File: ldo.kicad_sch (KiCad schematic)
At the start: 4 parts, among them U501 SPX3819M5-L-3-3

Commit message: Update to kicad 9
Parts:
- C502: value 10n -> 10n
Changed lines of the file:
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@@
 (kicad_sch
-	(version 20231120)
+	(version 20250114)
 	(generator "eeschema")
-	(generator_version "8.0")
+	(generator_version "9.0")
 	(paper "A5")
 	(junction
@@
 	(label "BYP"
 		(at 93.98 63.5 0)
-		(fields_autoplaced yes)
 		(effects
 			(font
@@
 		(shape input)
 		(at 62.23 60.96 180)
-		(fields_autoplaced yes)
 		(effects
 			(font
@@
 		(shape output)
 		(at 119.38 60.96 0)
-		(fields_autoplaced yes)
 		(effects
 			(font
@@
 			)
 		)
-		(property "Value" "10n	"
+		(property "Value" "10n"
 			(at 96.52 69.85 0)
 			(effects

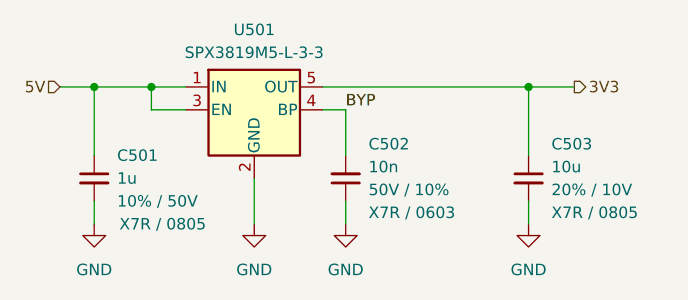
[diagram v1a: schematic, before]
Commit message: Update reference designators to single digit
Fits on the silk better
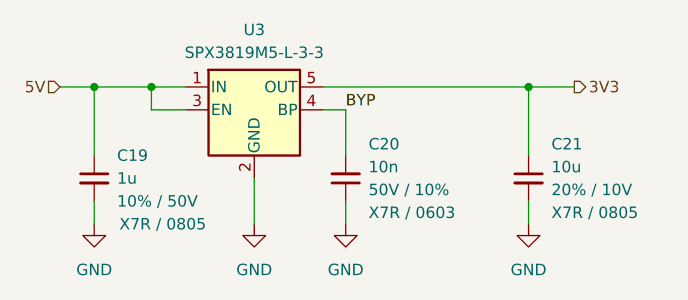
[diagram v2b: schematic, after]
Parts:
- renumbered C501 to C19, C502 to C20, C503 to C21, U501 to U3
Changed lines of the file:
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@@
 		(dnp no)
 		(fields_autoplaced yes)
-		(property "Reference" "#PWR0503"
+		(property "Reference" "#PWR033"
 			(at 93.98 82.55 0)
 			(effects
@@
 			(project "youdbetterrun"
 				(path "/50da2b4e-34b1-4787-8ee6-5d7d17f804f4/36ef99fe-a89f-4e2b-807e-d0c916080945"
-					(reference "#PWR0503")
+					(reference "#PWR033")
 					(unit 1)
 				)
@@
 		(on_board yes)
 		(dnp no)
-		(property "Reference" "C501"
+		(property "Reference" "C19"
 			(at 68.58 68.58 0)
 			(effects
@@
 			(project "youdbetterrun"
 				(path "/50da2b4e-34b1-4787-8ee6-5d7d17f804f4/36ef99fe-a89f-4e2b-807e-d0c916080945"
-					(reference "C501")
+					(reference "C19")
 					(unit 1)
 				)
@@
 		(dnp no)
 		(fields_autoplaced yes)
-		(property "Reference" "#PWR0504"
+		(property "Reference" "#PWR034"
 			(at 114.3 82.55 0)
 			(effects
@@
 			(project "youdbetterrun"
 				(path "/50da2b4e-34b1-4787-8ee6-5d7d17f804f4/36ef99fe-a89f-4e2b-807e-d0c916080945"
-					(reference "#PWR0504")
+					(reference "#PWR034")
 					(unit 1)
 				)
@@
 		(dnp no)
 		(fields_autoplaced yes)
-		(property "Reference" "U501"
+		(property "Reference" "U3"
 			(at 83.82 54.61 0)
 			(effects
@@
 			(project "youdbetterrun"
 				(path "/50da2b4e-34b1-4787-8ee6-5d7d17f804f4/36ef99fe-a89f-4e2b-807e-d0c916080945"
-					(reference "U501")
+					(reference "U3")
 					(unit 1)
 				)
@@
 		(on_board yes)
 		(dnp no)
-		(property "Reference" "C502"
+		(property "Reference" "C20"
 			(at 96.52 67.31 0)
 			(effects
@@
 			(project "youdbetterrun"
 				(path "/50da2b4e-34b1-4787-8ee6-5d7d17f804f4/36ef99fe-a89f-4e2b-807e-d0c916080945"
-					(reference "C502")
+					(reference "C20")
 					(unit 1)
 				)
@@
 		(on_board yes)
 		(dnp no)
-		(property "Reference" "C503"
+		(property "Reference" "C21"
 			(at 116.84 67.31 0)
 			(effects
@@
 			(project "youdbetterrun"
 				(path "/50da2b4e-34b1-4787-8ee6-5d7d17f804f4/36ef99fe-a89f-4e2b-807e-d0c916080945"
-					(reference "C503")
+					(reference "C21")
 					(unit 1)
 				)
@@
 		(dnp no)
 		(fields_autoplaced yes)
-		(property "Reference" "#PWR0501"
+		(property "Reference" "#PWR031"
 			(at 66.04 82.55 0)
 			(effects
@@
 			(project "youdbetterrun"
 				(path "/50da2b4e-34b1-4787-8ee6-5d7d17f804f4/36ef99fe-a89f-4e2b-807e-d0c916080945"
-					(reference "#PWR0501")
+					(reference "#PWR031")
 					(unit 1)
 				)
@@
 		(dnp no)
 		(fields_autoplaced yes)
-		(property "Reference" "#PWR0502"
+		(property "Reference" "#PWR032"
 			(at 83.82 82.55 0)
 			(effects
@@
 			(project "youdbetterrun"
 				(path "/50da2b4e-34b1-4787-8ee6-5d7d17f804f4/36ef99fe-a89f-4e2b-807e-d0c916080945"
-					(reference "#PWR0502")
-					(unit 1)
-				)
+					(reference "#PWR032")
+					(unit 1)
+				)

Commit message: Lighthouse
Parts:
- added C8, C9: 22u, Capacitor_THT:C_Radial_D5.0mm_H5.0mm_P2.00mm, symbol Device:C_Polarized_Small
- added D2, D3: MBR120, Diode_SMD:D_SOD-123F, symbol Device:D_Schottky_Small
- added J5: 694106301002, Connector_BarrelJack:BarrelJack_Wuerth_6941xx301002, symbol Connector:Barrel_Jack_Switch
- added J6: From_E-stop, TerminalBlock:TerminalBlock_MaiXu_MX126-5.0-02P_1x02_P5.00mm, symbol Connector:Screw_Terminal_01x02
- added U4: R-78E5.0-1.0, Converter_DCDC:Converter_DCDC_RECOM_R-78E-0.5_THT, symbol Regulator_Switching:R-78E3.3-1.0
- renumbered C19 to C10, C20 to C11, C21 to C12, U3 to U5
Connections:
- net 5V: now also D2.1 (K), D3.1 (K)
- net GND: now also C8.2, C9.2, J5.2, J5.3, J6.2 (Pin_2), U4.2 (GND)
- new net PWR: C8.1, J5.1, J6.1 (Pin_1), U4.1 (IN)
- new net VREG_OUT: C9.1, D3.2 (A), U4.3 (OUT)
- new net VUSB: D2.2 (A)
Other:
- company: (none) -> Marcel Robitaille
- title: (none) -> Power
- moved on the sheet: C10, C11, C12, U5

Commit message: Termianl block 3d view
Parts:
- J6: value From_E-stop -> TB0010-500-02GR; footprint TerminalBlock:TerminalBlock_MaiXu_MX126-5.0-02P_1x02_P5.00mm -> lighthouse:TerminalBlock_TB0010-500-02GR_1x02_P5.00mm
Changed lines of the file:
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@@
 			)
 		)
-		(property "Value" "From_E-stop"
+		(property "Value" "TB0010-500-02GR"
 			(at 35.56 44.45 0)
 			(effects
@@
 			)
 		)
-		(property "Footprint" "TerminalBlock:TerminalBlock_MaiXu_MX126-5.0-02P_1x02_P5.00mm"
+		(property "Footprint" "lighthouse:TerminalBlock_TB0010-500-02GR_1x02_P5.00mm"
 			(at 35.56 48.26 0)
 			(effects

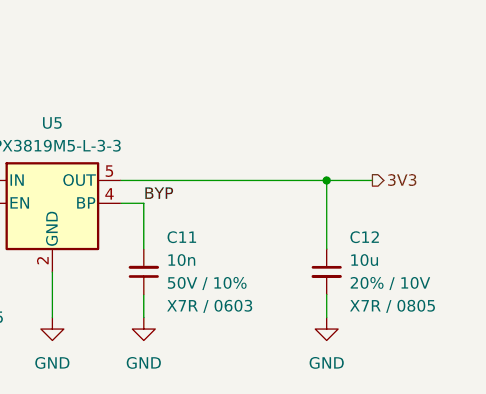
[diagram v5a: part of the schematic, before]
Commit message: Add component attributes
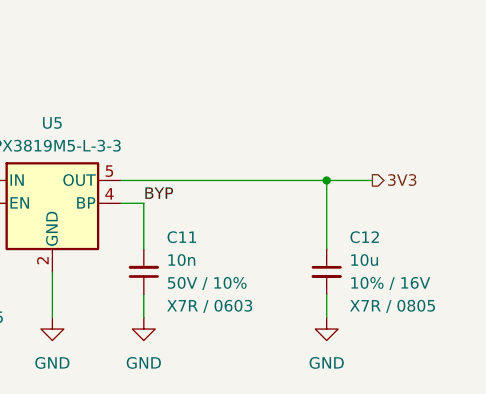
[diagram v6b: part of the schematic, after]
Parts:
- C12: LCSC Part Number C5189822 -> (none); MPN CS2012X7R106M100NRE -> CL21A106KOQNNNE; Manufacturer Samwha Capacitor -> Samsung Electro-Mechanics; Mouser Part Number (none) -> 187-CL21A106KOQNNNE; Rated Voltage 10V -> 16V; Tolerance 20% -> 10%
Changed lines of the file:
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@@
+			)
+		)
+		(property "Manufactuer" ""
+			(at 101.6 71.12 0)
+			(effects
+				(font
+					(size 1.27 1.27)
+				)
+				(hide yes)
 			)
 		)
@@
 			)
 		)
+		(property "Manufactuer" ""
+			(at 53.34 66.04 0)
+			(effects
+				(font
+					(size 1.27 1.27)
+				)
+				(hide yes)
+			)
+		)
 		(pin "2"
 		)
@@
 			)
 		)
+		(property "Manufactuer" ""
+			(at 73.66 66.04 0)
+			(effects
+				(font
+					(size 1.27 1.27)
+				)
+				(hide yes)
+			)
+		)
 		(pin "2"
 		)
@@
 			)
 		)
+		(property "Manufactuer" ""
+			(at 86.36 60.96 0)
+			(effects
+				(font
+					(size 1.27 1.27)
+				)
+				(hide yes)
+			)
+		)
 		(pin "2"
 		)
@@
 			)
 		)
+		(property "Manufactuer" ""
+			(at 33.02 63.5 0)
+			(effects
+				(font
+					(size 1.27 1.27)
+				)
+				(hide yes)
+			)
+		)
 		(pin "2"
 		)
@@
 			)
 		)
+		(property "Manufactuer" ""
+			(at 35.56 48.26 0)
+			(effects
+				(font
+					(size 1.27 1.27)
+				)
+				(hide yes)
+			)
+		)
 		(pin "1"
 		)
@@
 			)
 		)
+		(property "Manufactuer" ""
+			(at 86.36 50.8 0)
+			(effects
+				(font
+					(size 1.27 1.27)
+				)
+				(hide yes)
+			)
+		)
 		(pin "2"
 		)
@@
 			)
 		)
+		(property "Manufactuer" ""
+			(at 63.5 60.96 0)
+			(effects
+				(font
+					(size 1.27 1.27)
+				)
+				(hide yes)
+			)
+		)
 		(pin "3"
 		)
@@
 			)
 		)
+		(property "Manufactuer" ""
+			(at 119.38 63.5 0)
+			(effects
+				(font
+					(size 1.27 1.27)
+				)
+				(hide yes)
+			)
+		)
 		(pin "1"
 		)
@@
 		)
 		(property "Tolerance" "10%"
+			(at 129.54 71.12 0)
+			(effects
+				(font
+					(size 1.27 1.27)
+				)
+				(hide yes)
+			)
+		)
+		(property "Manufactuer" ""
 			(at 129.54 71.12 0)
 			(effects
@@
 			)
 		)
-		(property "LCSC Part Number" "C5189822"
+		(property "LCSC Part Number" ""
 			(at 149.86 71.12 0)
 			(effects
@@
 			)
 		)
-		(property "MPN" "CS2012X7R106M100NRE"
+		(property "MPN" "CL21A106KOQNNNE"
 			(at 149.86 71.12 0)
 			(effects
@@
 			)
 		)
-		(property "Manufacturer" "Samwha Capacitor"
+		(property "Manufacturer" "Samsung Electro-Mechanics"
 			(at 149.86 71.12 0)
 			(effects
@@
 			)
 		)
-		(property "Rated Voltage" "10V"
+		(property "Rated Voltage" "16V"
 			(at 149.86 71.12 0)
 			(effects
@@
 			)
 		)
-		(property "Tolerance" "20%"
+		(property "Tolerance" "10%"
 			(at 149.86 71.12 0)
 			(effects
@@
 			)
 		)
-		(property "Mouser Part Number" ""
+		(property "Mouser Part Number" "187-CL21A106KOQNNNE"
 			(at 149.86 71.12 0)
 			(effects
+				(font
+					(size 1.27 1.27)
+				)
+				(hide yes)
+			)
+		)
+		(property "Manufactuer" ""
+			(at 149.86 71.12 0)
+			(effects
